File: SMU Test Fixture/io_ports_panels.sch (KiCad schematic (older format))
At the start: 28 parts, among them J10 Ext. Source, J11 Scope 1+, J12 Scope 2+, J13 Conn_01x03, J4 WG1, J5 WG2, J6 105-1102-001, J7 105-1102-001, J8 Scope 1-, J9 Scope 2-, K27 50 Ohm Ena, K28 Ext Meas Sel B, K29 Ext Meas Sel A, K30 Single/Diff Switch, K31 AC/DC Couple, K32 AC/DC Couple B, K33 AC/DC Couple A

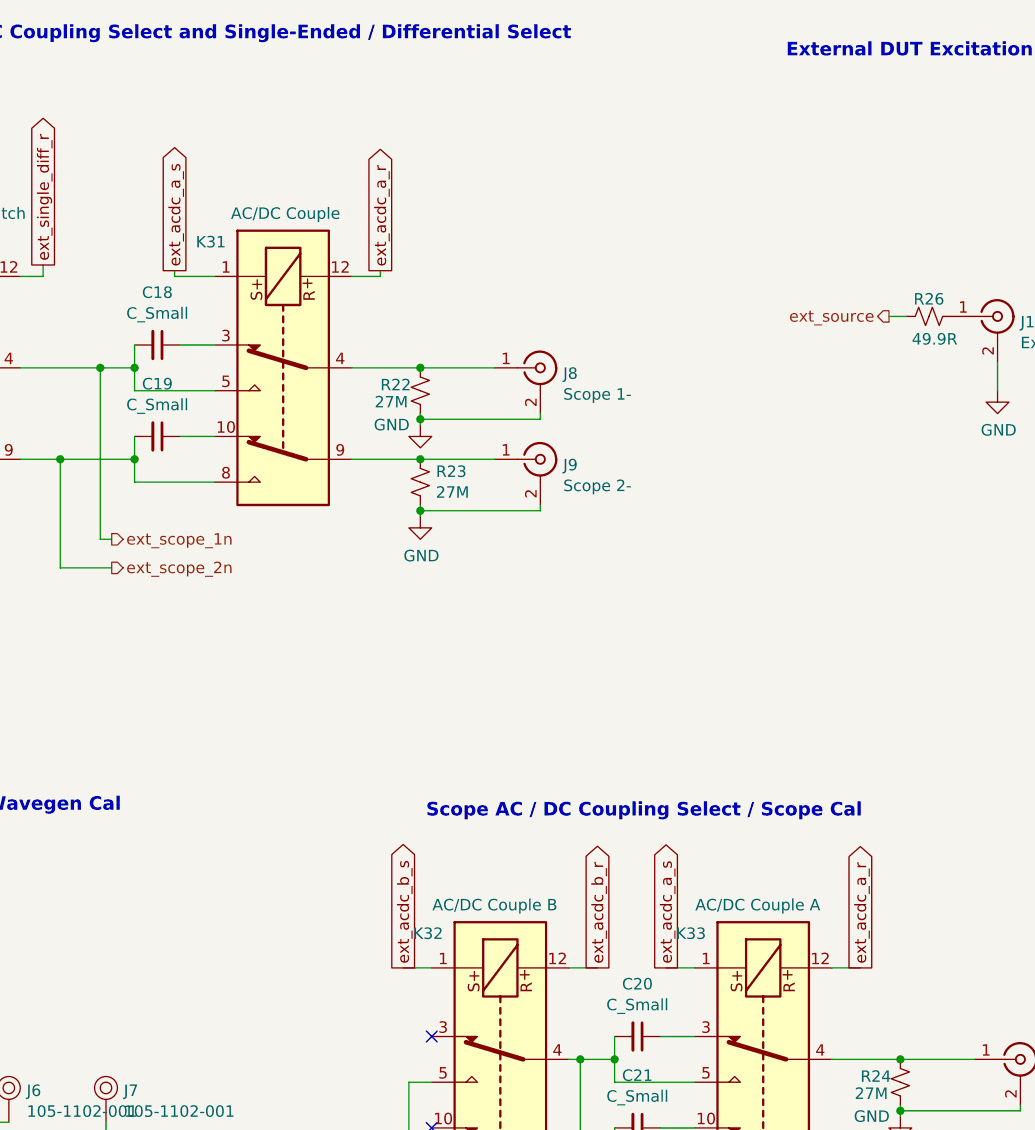
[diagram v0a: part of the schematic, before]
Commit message: Add simulations and relay state spreadsheet
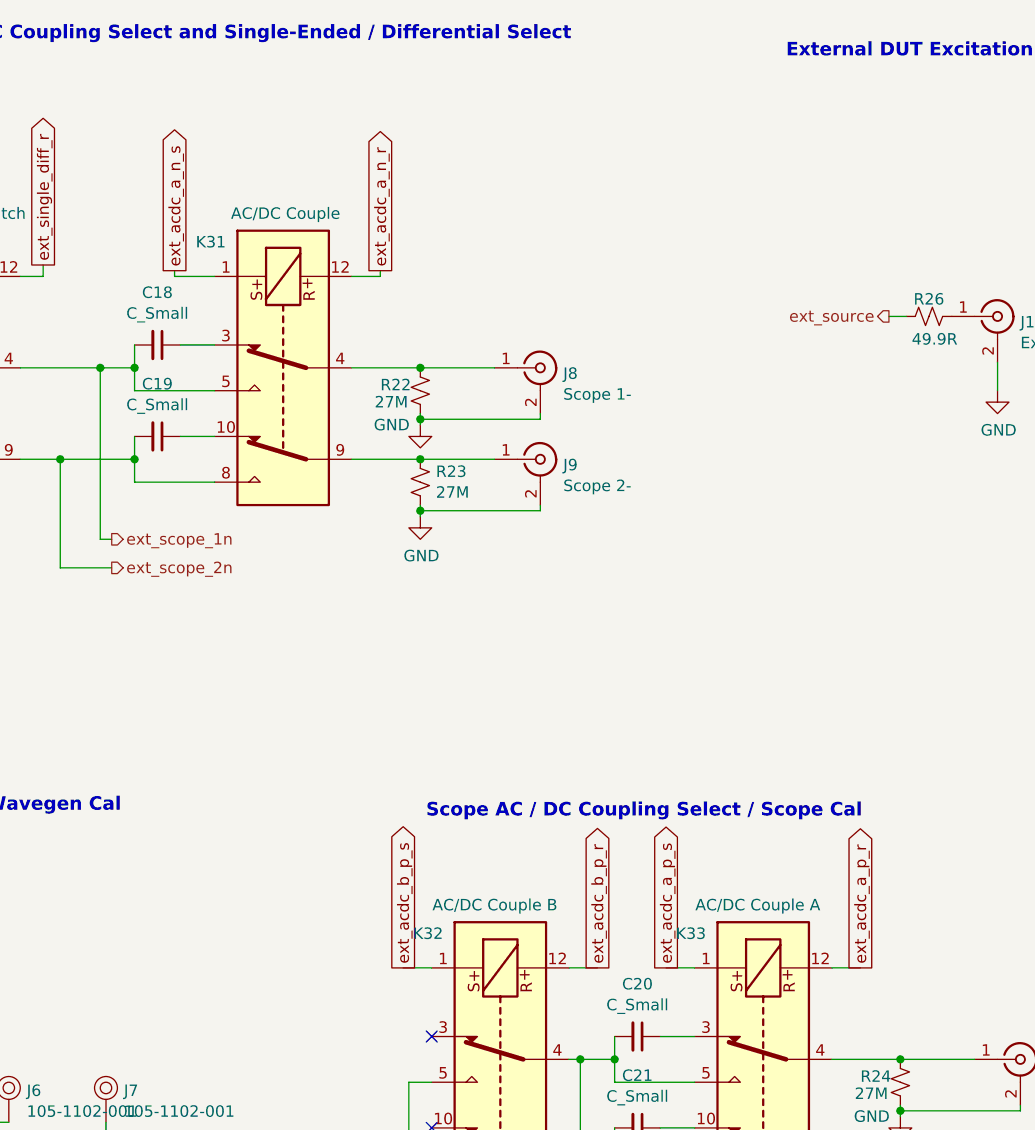
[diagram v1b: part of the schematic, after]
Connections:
- net ext_acdc_a_r renamed ext_acdc_a_n_r
- net ext_acdc_a_n_r: no longer K33.12
- net ext_acdc_a_s renamed ext_acdc_a_n_s
- net ext_acdc_a_n_s: no longer K33.1
- net ext_acdc_b_r renamed ext_acdc_b_p_r
- net ext_acdc_b_s renamed ext_acdc_b_p_s
- new net ext_acdc_a_p_r: K33.12
- new net ext_acdc_a_p_s: K33.1
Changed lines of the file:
@@
 	2800 1575 2675 1575
 Text GLabel 7600 4800 1    50   Output ~ 0
-ext_acdc_a_s
+ext_acdc_a_p_s
 Wire Wire Line
 	7600 4800 7725 4800
 Text GLabel 8450 4800 1    50   Output ~ 0
-ext_acdc_a_r
+ext_acdc_a_p_r
 Wire Wire Line
 	8450 4800 8325 4800
@@
 ext_meas_sel_b_r
 Text GLabel 6450 4800 1    50   Output ~ 0
-ext_acdc_b_s
+ext_acdc_b_p_s
 Text GLabel 7300 4800 1    50   Output ~ 0
-ext_acdc_b_r
+ext_acdc_b_p_r
 Wire Wire Line
 	6450 4800 6575 4800
@@
 	7175 4800 7300 4800
 Text GLabel 5450 1750 1    50   Output ~ 0
-ext_acdc_a_s
+ext_acdc_a_n_s
 Text GLabel 6350 1750 1    50   Output ~ 0
-ext_acdc_a_r
+ext_acdc_a_n_r
 Wire Wire Line
 	5450 1775 5450 1750

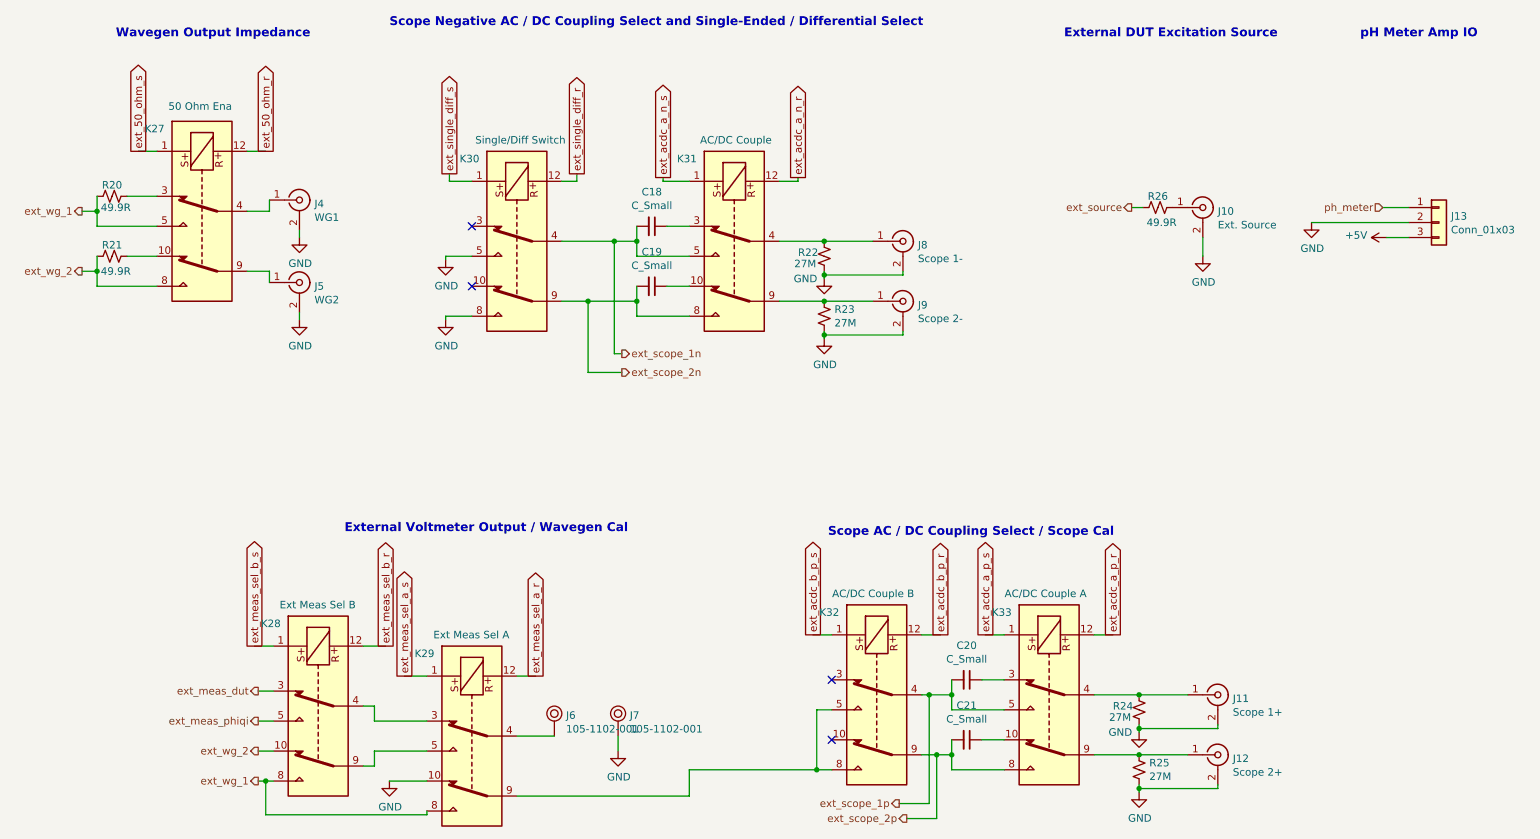
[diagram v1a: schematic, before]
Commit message: Elminate extra scope cal relay, re-organize relays, re-annotate, ERC
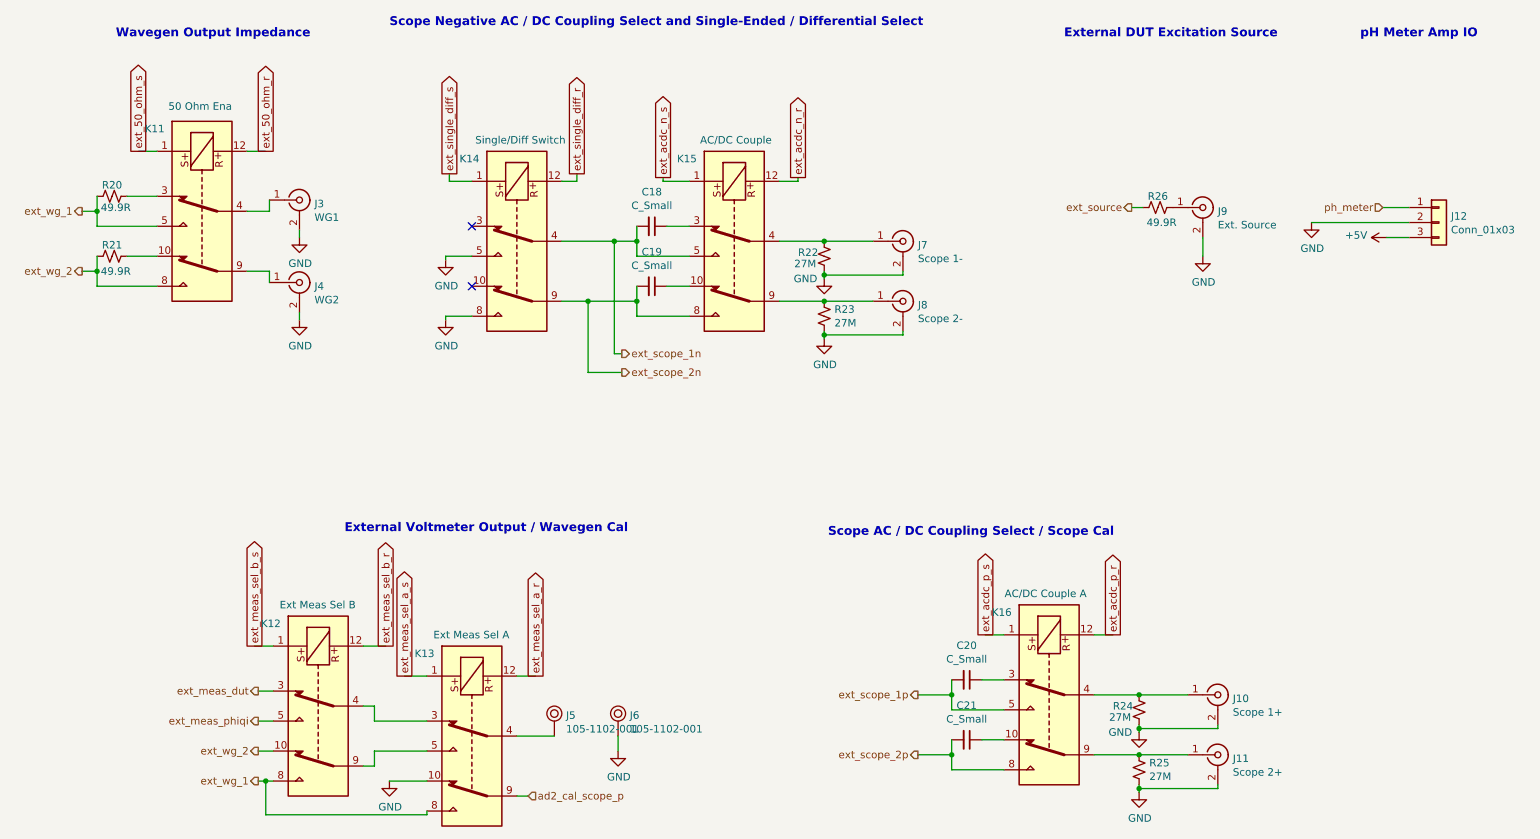
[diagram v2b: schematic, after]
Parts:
- removed K32: AC/DC Couple B, Relay_SMD:Relay_DPDT_Kemet_EE2_NUH, symbol Relay:EE2-12SNUH
- renumbered J11 to J10, J12 to J11, J13 to J12, J4 to J3, J5 to J4, J6 to J5, J7 to J6, J8 to J7, J9 to J8, J10 to J9, K27 to K11, K28 to K12, K29 to K13, K30 to K14, K31 to K15, K33 to K16
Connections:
- net ad2_cal_scope_p: now reaches K13.9
- net ext_acdc_a_n_r renamed ext_acdc_n_r
- net ext_acdc_a_n_s renamed ext_acdc_n_s
- net ext_acdc_a_p_r renamed ext_acdc_p_r
- net ext_acdc_a_p_s renamed ext_acdc_p_s
- no-connect marks 4 -> 2
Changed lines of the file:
@@
 $Descr A4 11693 8268
 encoding utf-8
-Sheet 5 8
+Sheet 4 8
 Title "I / O and Panel"
 Date "2020-11-29"
@@
 $EndDescr
 $Comp
-L Connector:Conn_Coaxial J4
+L Connector:Conn_Coaxial J3
 U 1 1 60665C26
 P 3025 1900
-AR Path="/5FC2AF5A/60665C26" Ref="J4"  Part="1"
+AR Path="/5FC2AF5A/60665C26" Ref="J3"  Part="1"
 AR Path="/60665C26" Ref="J?"  Part="1"
-F 0 "J4" H 3125 1875 50  0000 L CNN
+F 0 "J3" H 3125 1875 50  0000 L CNN
 F 1 "WG1" H 3125 1784 50  0000 L CNN
 F 2 "" H 3025 1900 50  0001 C CNN
@@
 $EndComp
 $Comp
-L Connector:Conn_Coaxial J11
+L Connector:Conn_Coaxial J10
 U 1 1 60665C2C
 P 9150 5200
-AR Path="/5FC2AF5A/60665C2C" Ref="J11"  Part="1"
+AR Path="/5FC2AF5A/60665C2C" Ref="J10"  Part="1"
 AR Path="/60665C2C" Ref="J?"  Part="1"
-F 0 "J11" H 9250 5175 50  0000 L CNN
+F 0 "J10" H 9250 5175 50  0000 L CNN
 F 1 "Scope 1+" H 9250 5084 50  0000 L CNN
 F 2 "" H 9150 5200 50  0001 C CNN
@@
 $EndComp
 $Comp
-L Connector:Conn_Coaxial J5
+L Connector:Conn_Coaxial J4
 U 1 1 60665C32
 P 3025 2450
-AR Path="/5FC2AF5A/60665C32" Ref="J5"  Part="1"
+AR Path="/5FC2AF5A/60665C32" Ref="J4"  Part="1"
 AR Path="/60665C32" Ref="J?"  Part="1"
-F 0 "J5" H 3125 2425 50  0000 L CNN
+F 0 "J4" H 3125 2425 50  0000 L CNN
 F 1 "WG2" H 3125 2334 50  0000 L CNN
 F 2 "" H 3025 2450 50  0001 C CNN
@@
 $EndComp
 $Comp
-L Connector:Conn_Coaxial J12
+L Connector:Conn_Coaxial J11
 U 1 1 60665C38
 P 9150 5600
-AR Path="/5FC2AF5A/60665C38" Ref="J12"  Part="1"
+AR Path="/5FC2AF5A/60665C38" Ref="J11"  Part="1"
 AR Path="/60665C38" Ref="J?"  Part="1"
-F 0 "J12" H 9250 5575 50  0000 L CNN
+F 0 "J11" H 9250 5575 50  0000 L CNN
 F 1 "Scope 2+" H 9250 5484 50  0000 L CNN
 F 2 "" H 9150 5600 50  0001 C CNN
@@
 $EndComp
 $Comp
-L Connector:Conn_Coaxial J10
+L Connector:Conn_Coaxial J9
 U 1 1 60665C3E
 P 9050 1950
-AR Path="/5FC2AF5A/60665C3E" Ref="J10"  Part="1"
+AR Path="/5FC2AF5A/60665C3E" Ref="J9"  Part="1"
 AR Path="/60665C3E" Ref="J?"  Part="1"
-F 0 "J10" H 9150 1925 50  0000 L CNN
+F 0 "J9" H 9150 1925 50  0000 L CNN
 F 1 "Ext. Source" H 9150 1834 50  0000 L CNN
 F 2 "" H 9050 1950 50  0001 C CNN
@@
 $EndComp
 $Comp
-L dk_Banana-and-Tip-Connectors-Jacks-Plugs:105-1102-001 J6
+L dk_Banana-and-Tip-Connectors-Jacks-Plugs:105-1102-001 J5
 U 1 1 60665C4D
 P 4725 5325
-AR Path="/5FC2AF5A/60665C4D" Ref="J6"  Part="1"
+AR Path="/5FC2AF5A/60665C4D" Ref="J5"  Part="1"
 AR Path="/60665C4D" Ref="J?"  Part="1"
-F 0 "J6" H 4803 5313 50  0000 L CNN
+F 0 "J5" H 4803 5313 50  0000 L CNN
 F 1 "105-1102-001" H 4803 5222 50  0000 L CNN
 F 2 "digikey-footprints:Test_Jack_Horiz" H 4925 5525 60  0001 L CNN
@@
 $EndComp
 $Comp
-L dk_Banana-and-Tip-Connectors-Jacks-Plugs:105-1102-001 J7
+L dk_Banana-and-Tip-Connectors-Jacks-Plugs:105-1102-001 J6
 U 1 1 60665C5C
 P 5150 5325
-AR Path="/5FC2AF5A/60665C5C" Ref="J7"  Part="1"
+AR Path="/5FC2AF5A/60665C5C" Ref="J6"  Part="1"
 AR Path="/60665C5C" Ref="J?"  Part="1"
-F 0 "J7" H 5228 5313 50  0000 L CNN
+F 0 "J6" H 5228 5313 50  0000 L CNN
 F 1 "105-1102-001" H 5228 5222 50  0000 L CNN
 F 2 "digikey-footprints:Test_Jack_Horiz" H 5350 5525 60  0001 L CNN
@@
 AR Path="/62B74232/6066B19E" Ref="K?"  Part="1"
 AR Path="/6066B19E" Ref="K?"  Part="1"
-AR Path="/5FC2AF5A/6066B19E" Ref="K27"  Part="1"
-F 0 "K27" V 1825 2225 50  0000 L CNN
+AR Path="/5FC2AF5A/6066B19E" Ref="K11"  Part="1"
+F 0 "K11" V 1825 2225 50  0000 L CNN
 F 1 "50 Ohm Ena" V 1675 1775 50  0000 L CNN
 F 2 "Relay_SMD:Relay_DPDT_Kemet_EE2_NUH" H 2375 1975 50  0001 C CNN
@@
 AR Path="/62B74232/6066B92E" Ref="K?"  Part="1"
 AR Path="/6066B92E" Ref="K?"  Part="1"
-AR Path="/5FC2AF5A/6066B92E" Ref="K33"  Part="1"
-F 0 "K33" V 7475 5450 50  0000 L CNN
+AR Path="/5FC2AF5A/6066B92E" Ref="K16"  Part="1"
+F 0 "K16" V 7475 5450 50  0000 L CNN
 F 1 "AC/DC Couple A" V 7350 4950 50  0000 L CNN
 F 2 "Relay_SMD:Relay_DPDT_Kemet_EE2_NUH" H 8025 5200 50  0001 C CNN
@@
 	8625 5825 8625 5800
 Wire Wire Line
-	7025 5925 7225 5925
-Wire Wire Line
-	7075 6025 7275 6025
-Wire Wire Line
 	2075 1875 1875 1875
 Wire Wire Line
@@
 	2800 1575 2675 1575
 Text GLabel 7600 4800 1    50   Output ~ 0
-ext_acdc_a_p_s
+ext_acdc_p_s
 Wire Wire Line
 	7600 4800 7725 4800
 Text GLabel 8450 4800 1    50   Output ~ 0
-ext_acdc_a_p_r
+ext_acdc_p_r
 Wire Wire Line
 	8450 4800 8325 4800
@@
 $EndComp
 $Comp
-L Connector:Conn_Coaxial J8
+L Connector:Conn_Coaxial J7
 U 1 1 607A8690
 P 7050 2175
-AR Path="/5FC2AF5A/607A8690" Ref="J8"  Part="1"
+AR Path="/5FC2AF5A/607A8690" Ref="J7"  Part="1"
 AR Path="/607A8690" Ref="J?"  Part="1"
-F 0 "J8" H 7150 2150 50  0000 L CNN
+F 0 "J7" H 7150 2150 50  0000 L CNN
 F 1 "Scope 1-" H 7150 2059 50  0000 L CNN
 F 2 "" H 7050 2175 50  0001 C CNN
@@
 $EndComp
 $Comp
-L Connector:Conn_Coaxial J9
+L Connector:Conn_Coaxial J8
 U 1 1 607A8696
 P 7050 2575
-AR Path="/5FC2AF5A/607A8696" Ref="J9"  Part="1"
+AR Path="/5FC2AF5A/607A8696" Ref="J8"  Part="1"
 AR Path="/607A8696" Ref="J?"  Part="1"
-F 0 "J9" H 7150 2550 50  0000 L CNN
+F 0 "J8" H 7150 2550 50  0000 L CNN
 F 1 "Scope 2-" H 7150 2459 50  0000 L CNN
 F 2 "" H 7050 2575 50  0001 C CNN
@@
 AR Path="/62B74232/607A869D" Ref="K?"  Part="1"
 AR Path="/607A869D" Ref="K?"  Part="1"
-AR Path="/5FC2AF5A/607A869D" Ref="K31"  Part="1"
-F 0 "K31" V 5375 2425 50  0000 L CNN
+AR Path="/5FC2AF5A/607A869D" Ref="K15"  Part="1"
+F 0 "K15" V 5375 2425 50  0000 L CNN
 F 1 "AC/DC Couple" V 5250 1925 50  0000 L CNN
 F 2 "Relay_SMD:Relay_DPDT_Kemet_EE2_NUH" H 5925 2175 50  0001 C CNN
@@
 AR Path="/62B74232/607AF36B" Ref="K?"  Part="1"
 AR Path="/607AF36B" Ref="K?"  Part="1"
-AR Path="/5FC2AF5A/607AF36B" Ref="K30"  Part="1"
-F 0 "K30" V 3925 2425 50  0000 L CNN
+AR Path="/5FC2AF5A/607AF36B" Ref="K14"  Part="1"
+F 0 "K14" V 3925 2425 50  0000 L CNN
 F 1 "Single/Diff Switch" V 3800 1850 50  0000 L CNN
 F 2 "Relay_SMD:Relay_DPDT_Kemet_EE2_NUH" H 4475 2175 50  0001 C CNN
@@
 Text HLabel 5175 3050 2    50   Output ~ 0
 ext_scope_2n
-Text HLabel 7025 5925 0    50   Output ~ 0
+Text HLabel 7150 5200 0    50   Output ~ 0
 ext_scope_1p
-Text HLabel 7075 6025 0    50   Output ~ 0
+Text HLabel 7150 5600 0    50   Output ~ 0
 ext_scope_2p
 Text HLabel 1575 1975 0    50   Output ~ 0
@@
 	10250 1950 10425 1950
 $Comp
-L Connector_Generic:Conn_01x03 J13
+L Connector_Generic:Conn_01x03 J12
 U 1 1 60A5F96A
 P 10625 2050
-F 0 "J13" H 10705 2092 50  0000 L CNN
+F 0 "J12" H 10705 2092 50  0000 L CNN
 F 1 "Conn_01x03" H 10705 2001 50  0000 L CNN
 F 2 "" H 10625 2050 50  0001 C CNN
@@
 AR Path="/62B74232/60035407" Ref="K?"  Part="1"
 AR Path="/60035407" Ref="K?"  Part="1"
-AR Path="/5FC2AF5A/60035407" Ref="K28"  Part="1"
-F 0 "K28" V 2600 5525 50  0000 L CNN
+AR Path="/5FC2AF5A/60035407" Ref="K12"  Part="1"
+F 0 "K12" V 2600 5525 50  0000 L CNN
 F 1 "Ext Meas Sel B" V 2475 5025 50  0000 L CNN
 F 2 "Relay_SMD:Relay_DPDT_Kemet_EE2_NUH" H 3150 5275 50  0001 C CNN
@@
 	0    -1   -1   0
 $EndComp
-$Comp
-L Relay:EE2-12SNUH K?
-U 1 1 600A64CE
-P 6875 5200
-AR Path="/600C9795/600A64CE" Ref="K?"  Part="1"
-AR Path="/62B74232/600A64CE" Ref="K?"  Part="1"
-AR Path="/600A64CE" Ref="K?"  Part="1"
-AR Path="/5FC2AF5A/600A64CE" Ref="K32"  Part="1"
-F 0 "K32" V 6325 5450 50  0000 L CNN
-F 1 "AC/DC Couple B" V 6200 4950 50  0000 L CNN
-F 2 "Relay_SMD:Relay_DPDT_Kemet_EE2_NUH" H 6875 5200 50  0001 C CNN
-F 3 "https://content.kemet.com/datasheets/KEM_R7002_EC2_EE2.pdf" H 6875 5200 50  0001 C CNN
-F 4 "EC2-12SNU" V 6875 5200 50  0001 C CNN "PN"
-	1    6875 5200
-	0    -1   1    0
-$EndComp
 Wire Wire Line
 	7375 5100 7375 5200
 Wire Wire Line
 	7375 5500 7375 5600
-Wire Wire Line
-	7175 5200 7225 5200
 Connection ~ 7375 5200
 Wire Wire Line
 	7375 5200 7375 5300
-Wire Wire Line
-	7175 5600 7275 5600
 Connection ~ 7375 5600
 Wire Wire Line
 	7375 5600 7375 5700
-Wire Wire Line
-	6575 5300 6475 5300
-Wire Wire Line
-	6475 5300 6475 5700
-Wire Wire Line
-	6475 5700 6575 5700
 $Comp
 L Relay:EE2-12SNUH K?
@@
 AR Path="/62B74232/60697D2A" Ref="K?"  Part="1"
 AR Path="/60697D2A" Ref="K?"  Part="1"
-AR Path="/5FC2AF5A/60697D2A" Ref="K29"  Part="1"
-F 0 "K29" V 3625 5725 50  0000 L CNN
+AR Path="/5FC2AF5A/60697D2A" Ref="K13"  Part="1"
+F 0 "K13" V 3625 5725 50  0000 L CNN
 F 1 "Ext Meas Sel A" V 3500 5225 50  0000 L CNN
 F 2 "Relay_SMD:Relay_DPDT_Kemet_EE2_NUH" H 4175 5475 50  0001 C CNN
@@
 $EndComp
 Wire Wire Line
-	6475 5700 5625 5700
-Wire Wire Line
-	5625 5700 5625 5875
-Wire Wire Line
-	5625 5875 4475 5875
-Connection ~ 6475 5700
-Wire Wire Line
 	3625 5775 3875 5775
 Connection ~ 2800 5775
 Wire Wire Line
 	2800 5775 2850 5775
-Wire Wire Line
-	7225 5925 7225 5200
-Connection ~ 7225 5200
-Wire Wire Line
-	7225 5200 7375 5200
-Wire Wire Line
-	7275 6025 7275 5600
-Connection ~ 7275 5600
-Wire Wire Line
-	7275 5600 7375 5600
-NoConn ~ 6575 5100
-NoConn ~ 6575 5500
 $Comp
 L power:GND #PWR034
@@
 Text GLabel 3600 4875 1    50   Output ~ 0
 ext_meas_sel_b_r
-Text GLabel 6450 4800 1    50   Output ~ 0
-ext_acdc_b_p_s
-Text GLabel 7300 4800 1    50   Output ~ 0
-ext_acdc_b_p_r
-Wire Wire Line
-	6450 4800 6575 4800
-Wire Wire Line
-	7175 4800 7300 4800
 Text GLabel 5450 1750 1    50   Output ~ 0
-ext_acdc_a_n_s
+ext_acdc_n_s
 Text GLabel 6350 1750 1    50   Output ~ 0
-ext_acdc_a_n_r
+ext_acdc_n_r
 Wire Wire Line
 	5450 1775 5450 1750
@@
 Wire Wire Line
 	3450 4875 3600 4875
+Text HLabel 4550 5875 2    50   Input ~ 0
+ad2_cal_scope_p
+Wire Wire Line
+	4550 5875 4475 5875
+Wire Wire Line
+	7150 5200 7375 5200
+Wire Wire Line
+	7150 5600 7375 5600
 $EndSCHEMATC
